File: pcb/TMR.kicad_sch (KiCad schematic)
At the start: 4 parts, among them U4 TMR2652D

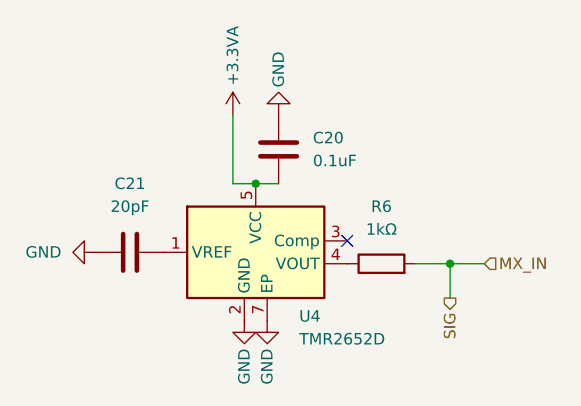
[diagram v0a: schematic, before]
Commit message: feat: completed layout for a single switch
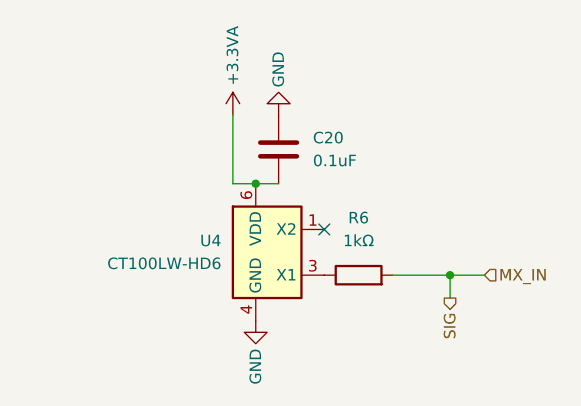
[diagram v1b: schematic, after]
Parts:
- removed C21: 20pF, Capacitor_SMD:C_0402_1005Metric, symbol Device:C
- removed U4: TMR2652D, prometheus-65-footprints:TMR2652D, symbol prometheus-65-symbols:TMR2652D
- added U4: CT100LW-HD6, prometheus-65-footprints:CT100LW-HD6, symbol prometheus-65-symbols:CT100LW-HD6
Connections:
- net +3.3VA: now also U4.6 (VDD)
- net GND: now also U4.4 (GND)
- net at R6.1: now also U4.3 (X1)
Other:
- moved on the sheet: R6
